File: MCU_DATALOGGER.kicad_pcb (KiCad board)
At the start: 2 copper layers, 28 parts, among them J1 Conn_01x04_Pin, J2 Conn_01x04_Pin, J3 Conn_01x09_Pin, J4 Conn_02x03_Odd_Even, U1 24LC1025, U2 24LC1025, U3 DS1337S_, U4 ATMEGA328P-AU, Y1 32.768 KHz, Y2 16 MHz

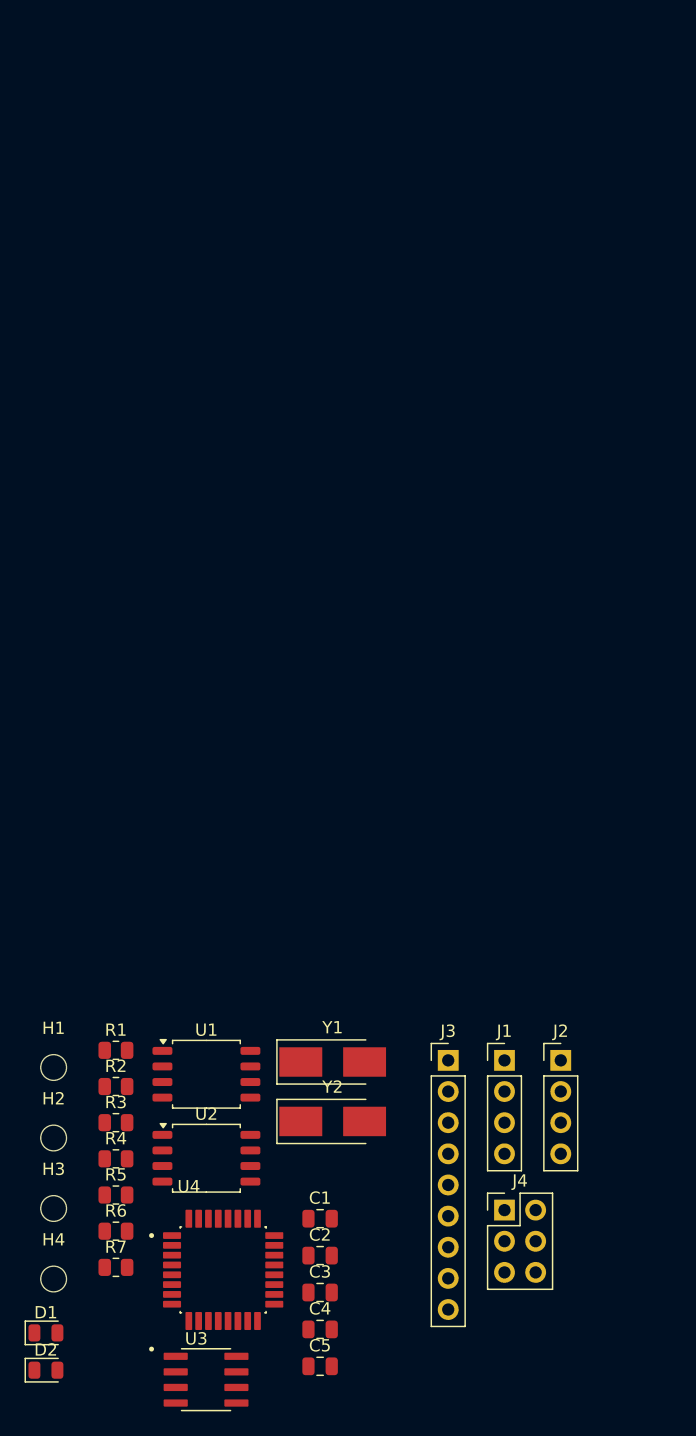
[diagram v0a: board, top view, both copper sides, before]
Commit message: Added & arranged footprints
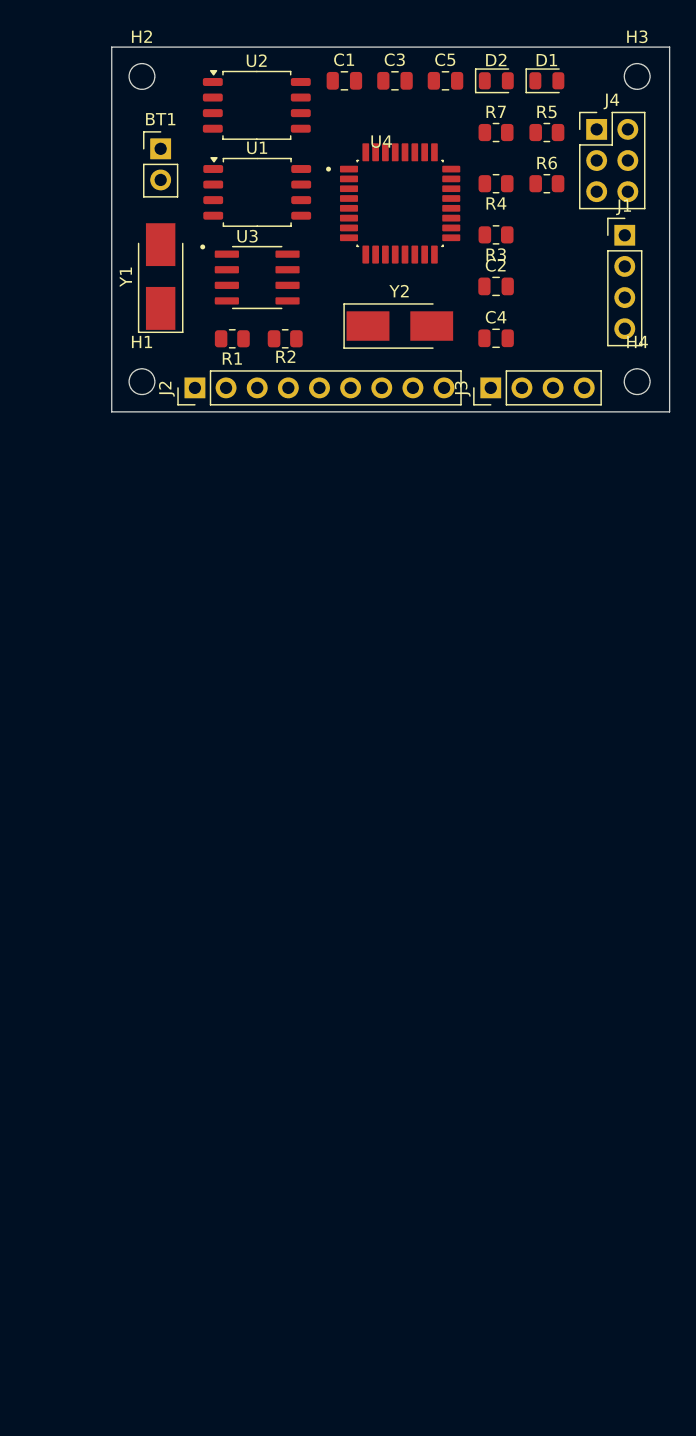
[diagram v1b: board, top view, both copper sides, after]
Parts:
- added BT1: Battery, Connector_PinHeader_2.54mm:PinHeader_1x02_P2.54mm_Vertical, F.Cu at (126.5, 78.5)
- moved D2 111.4 mm to (153.9, 73.0)
- moved D1 110.0 mm to (158.0, 73.0)
- moved C5 105.3 mm to (149.7, 73.0)
- moved H3 103.9 mm to (165.4, 72.6)
- moved C3 99.0 mm to (145.6, 73.0)
- moved R7 97.6 mm to (153.8, 77.2)
- moved R5 93.5 mm to (158.0, 77.2)
- moved C1 92.8 mm to (141.5, 73.0)
- moved R6 92.4 mm to (158.0, 81.4)
- moved U3 90.0 mm to (134.4, 89.0)
- moved J4 88.5 mm to (162.1, 77.0)
- moved U4 88.2 mm to (146.0, 83.0)
- moved H4 87.3 mm to (165.4, 97.5)
- moved H2 86.9 mm to (125.0, 72.6)
- moved U2 86.0 mm to (134.3, 75.0)
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- renumbered J3 to J2, J2 to J3
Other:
- board outline added: 45.5 x 29.8 mm

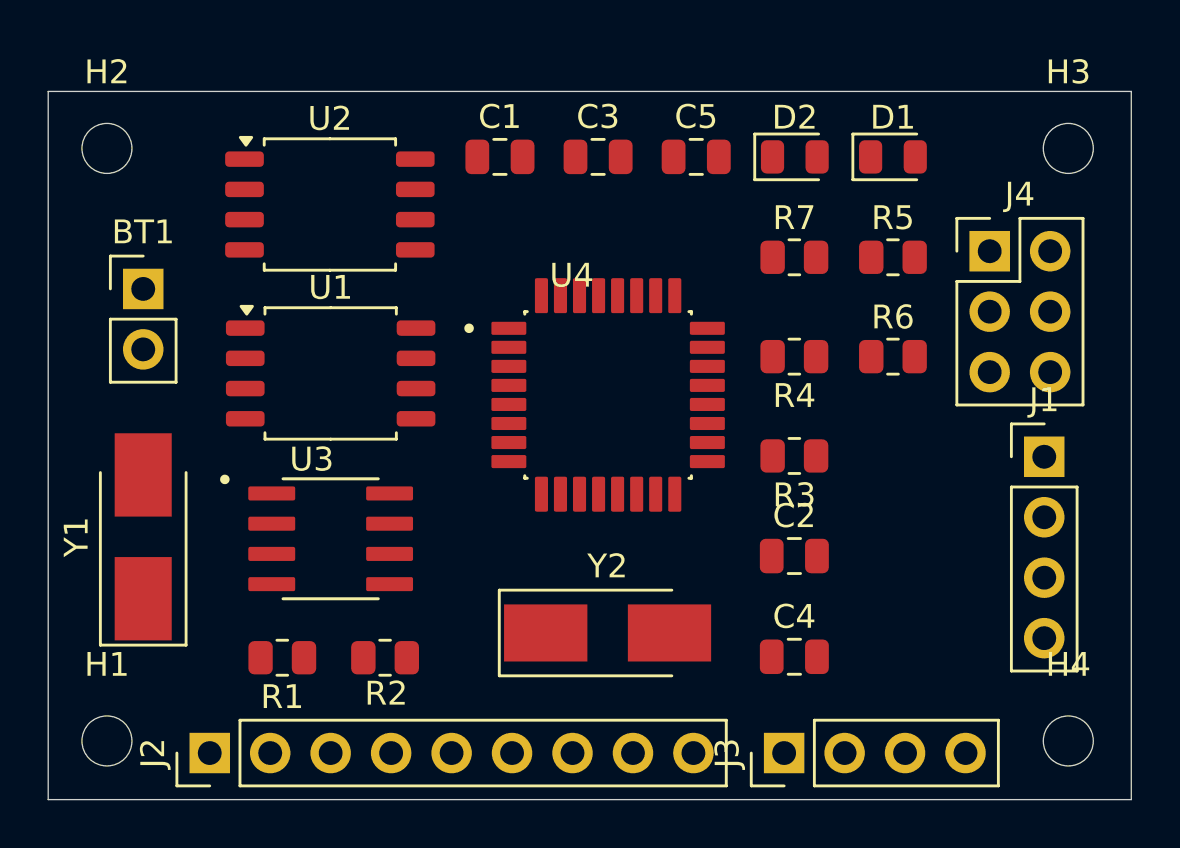
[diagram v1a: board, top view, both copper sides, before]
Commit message: Footprints routed in layout
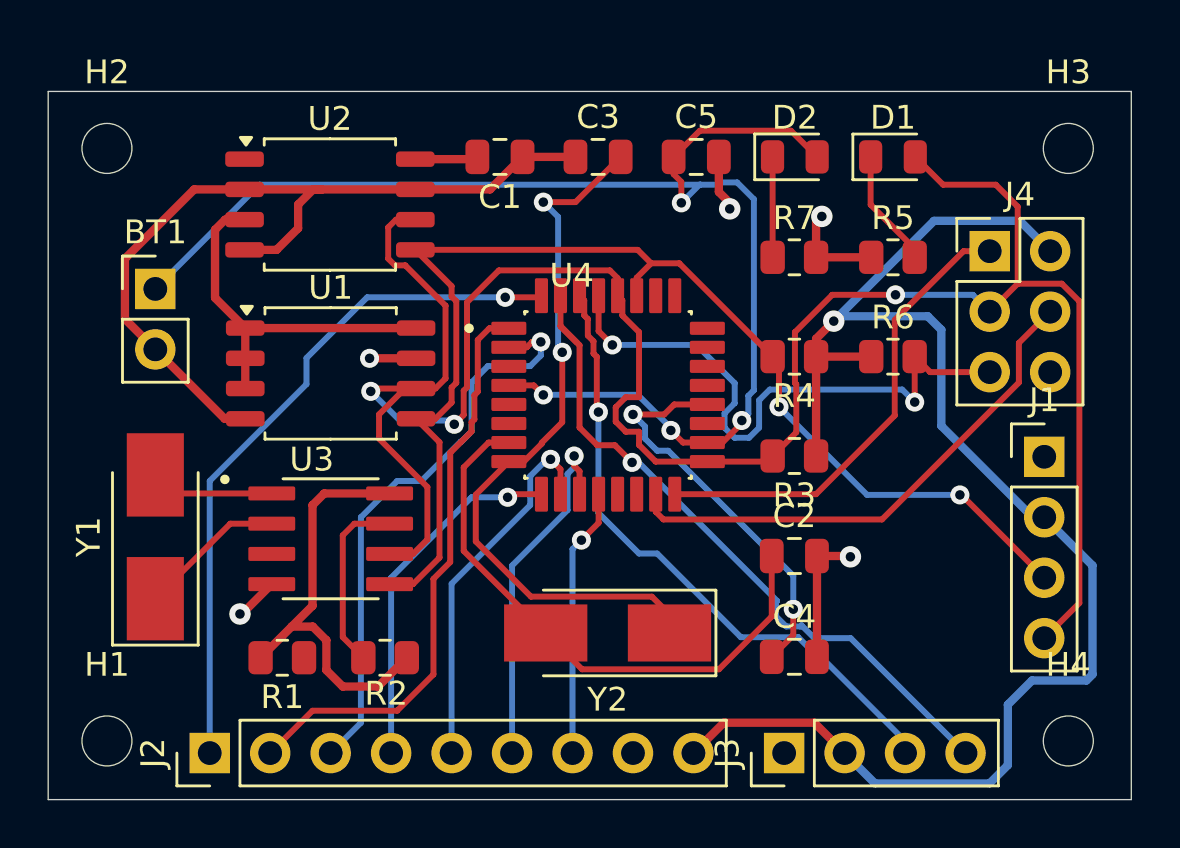
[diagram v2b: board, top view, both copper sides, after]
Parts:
- moved BT1 0.51 mm to (127.0, 78.5)
- moved Y1 0.51 mm to (127.0, 89.0)
- turned C1 to 180 degrees
- turned Y2 to 180 degrees
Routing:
- net /VCC: track 0.00 -> 99.9 mm, vias 0 -> 1
- net /SCK: track 0.00 -> 96.0 mm, vias 0 -> 3
- net Net-(BT1-+): track 0.00 -> 58.2 mm, vias 0 -> 4
- net /SDA: track 0.00 -> 52.6 mm, vias 0 -> 2
- net GND: track 0.00 -> 50.9 mm, vias 0 -> 5
- net Net-(U4-PB7): track 0.00 -> 30.7 mm, vias 0 -> 2
- net /D2: track 0.00 -> 29.2 mm, vias 0 -> 1
- net /TX: track 0.00 -> 29.2 mm, vias 0 -> 1
- net /RX: track 0.00 -> 26.8 mm, vias 0 -> 1
- net /RESET: track 0.00 -> 25.4 mm, vias 0 -> 2
- net /D3: track 0.00 -> 24.6 mm
- net Net-(U4-PB6): track 0.00 -> 24.3 mm
- net /D4: track 0.00 -> 24.0 mm, vias 0 -> 1
- net /MOSI: track 0.00 -> 22.0 mm
- net /MISO: track 0.00 -> 19.8 mm
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
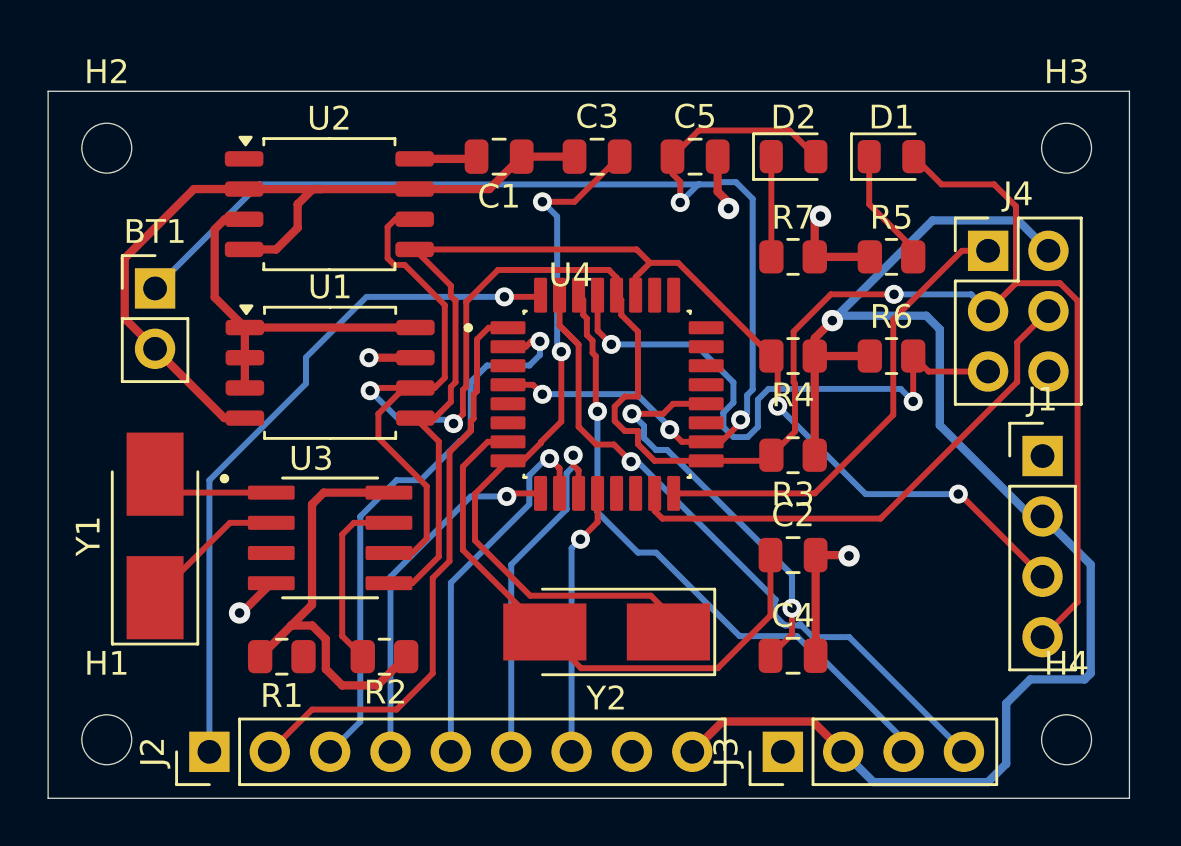
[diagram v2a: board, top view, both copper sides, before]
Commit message: Completed layout design of 2 layer
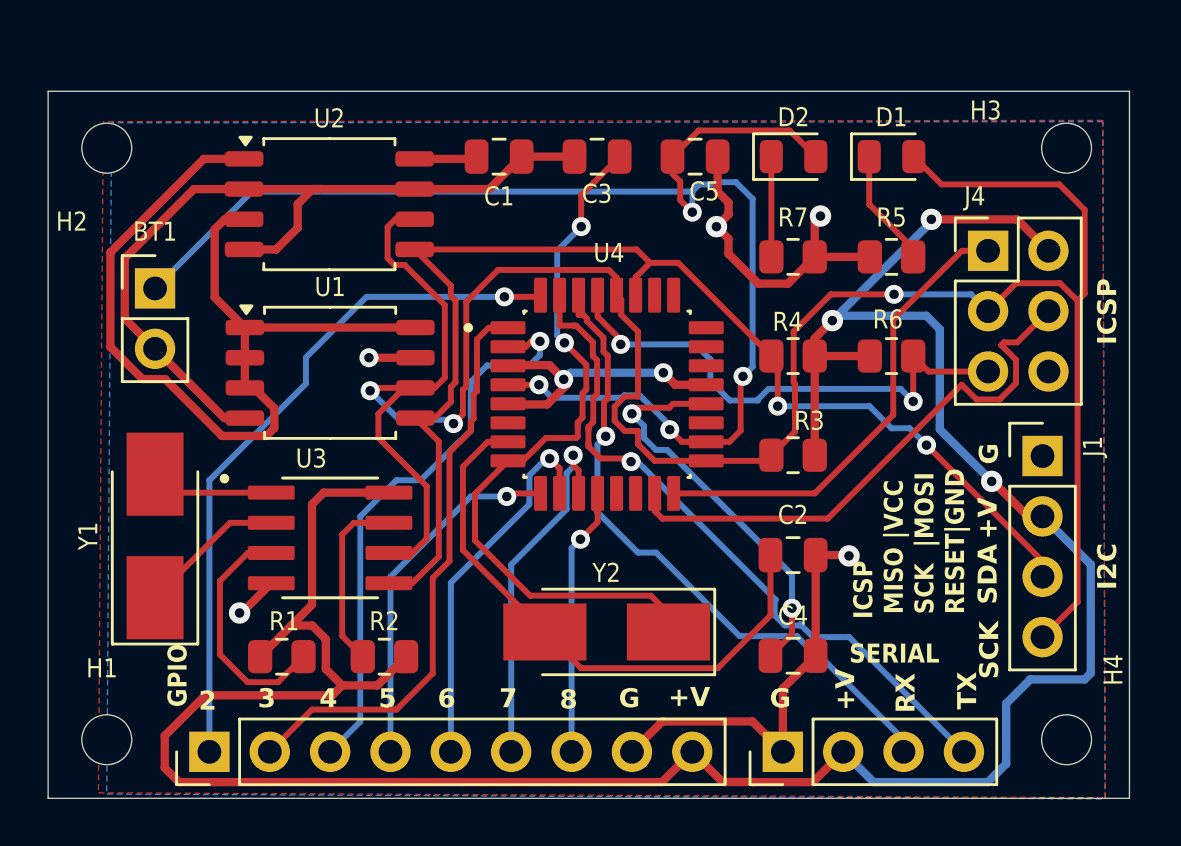
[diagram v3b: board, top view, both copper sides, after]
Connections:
- BT1 pad 1: Net-(BT1-+) -> /VCC
- C5 pad 1: Net-(BT1-+) -> /VCC
- D2 pad 2: Net-(BT1-+) -> /VCC
- U4 pad 18: Net-(BT1-+) -> /VCC
- U4 pad 4: Net-(BT1-+) -> /VCC
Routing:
- net /VCC: track 99.9 -> 215.1 mm, vias 1 -> 7
- net Net-(BT1-+): track 58.2 -> 0.00 mm, vias 4 -> 0
- net GND: track 50.9 -> 81.9 mm, vias 5 -> 7
- net Net-(U3-~{INTA}): track 0.00 -> 10.2 mm
- net /SCK: track 96.0 -> 99.6 mm
- net /RESET: track 25.4 -> 22.1 mm
- net /MOSI: track 22.0 -> 23.4 mm
- net /RX: track 26.8 -> 27.4 mm
- net Net-(U4-PB7): track 30.7 -> 31.2 mm
- added copper zone on F.Cu, net /VCC
- added copper zone on B.Cu, net GND
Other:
- board text added: "+V"
- board text added: "2"
- board text added: "3"
- board text added: "4"
- board text added: "5"
- board text added: "6"
- board text added: "7"
- board text added: "8"
- board text added: "A 2 Layer MCU Datalogger PCB"
- board text added: "G"
- board text added: "GPIO"
- board text added: "I2C"
- board text added: "ICSP"
- board text added: "MISO |VCC SCK |MOSI RESET|GND"
- board text added: "RX"
- board text added: "SCK"
- board text added: "SDA"
- board text added: "SERIAL"
- board text added: "TX"
- board text added: "~Designed By Shiv"
